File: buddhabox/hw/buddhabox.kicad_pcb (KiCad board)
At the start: 2 copper layers, 48.3 x 22.9 mm, 53 parts, among them J1 Serial, J2 SWD, J3 USB_B_Micro, J4 Speaker, J5 Battery, SW1 SW_Push, SW3 SW_Push, SW4 SW_Push, U1 TPS61291DRVR, U3 RP2040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

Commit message: Updated with working board design and pictures.
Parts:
- removed D2: LED Red, LED_SMD:LED_0603_1608Metric
- removed R5: 1k, Resistor_SMD:R_0402_1005Metric
- moved D3 16.8 mm to (129.1, 103.5), turned to -90 degrees
- moved C20 1.40 mm to (126.6, 118.0)
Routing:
- net Net-(D3-Pad2): track 1.51 -> 20.9 mm, vias 0 -> 2
- net +3.3V: track 107.9 -> 103.9 mm
- net GND: track 36.9 -> 35.5 mm
- net Net-(D2-Pad2): track 1.24 -> 0.00 mm
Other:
- board text removed: "PWR"

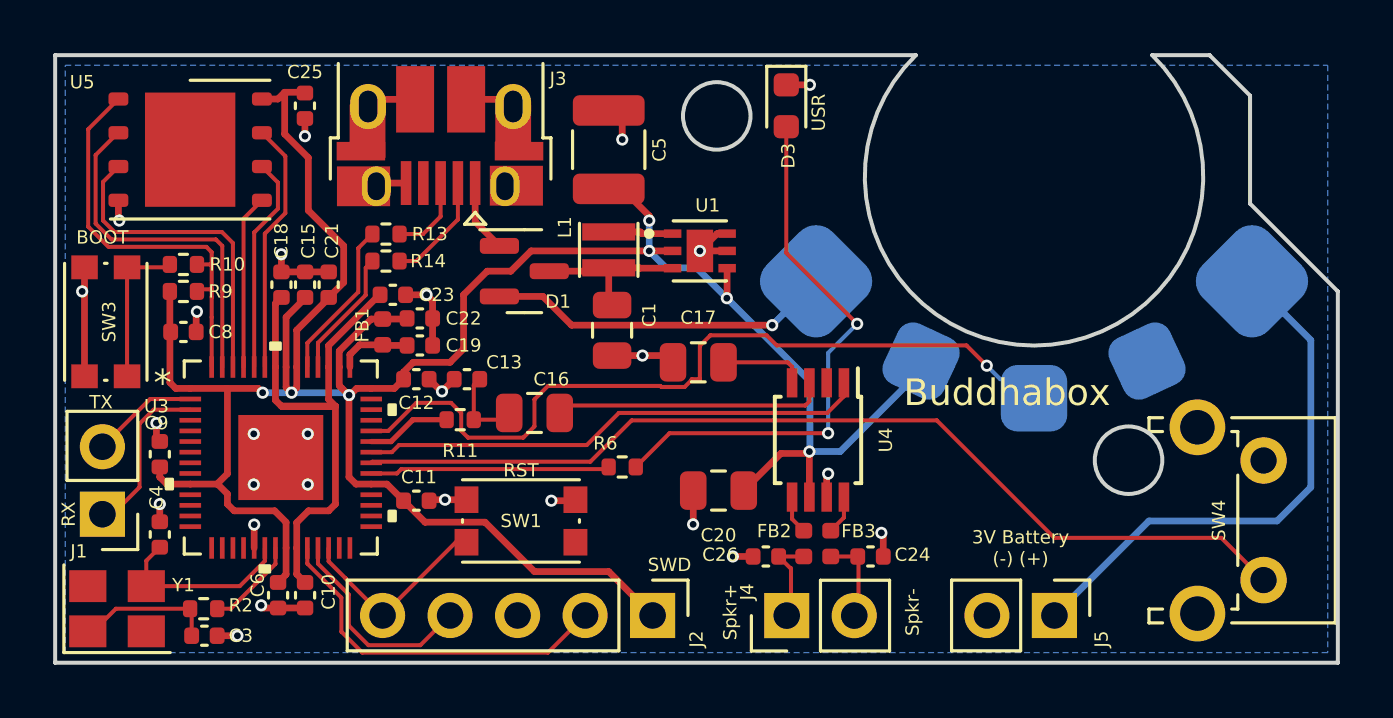
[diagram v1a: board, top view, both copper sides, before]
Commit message: switch to i2s amp & added LDO to vbus
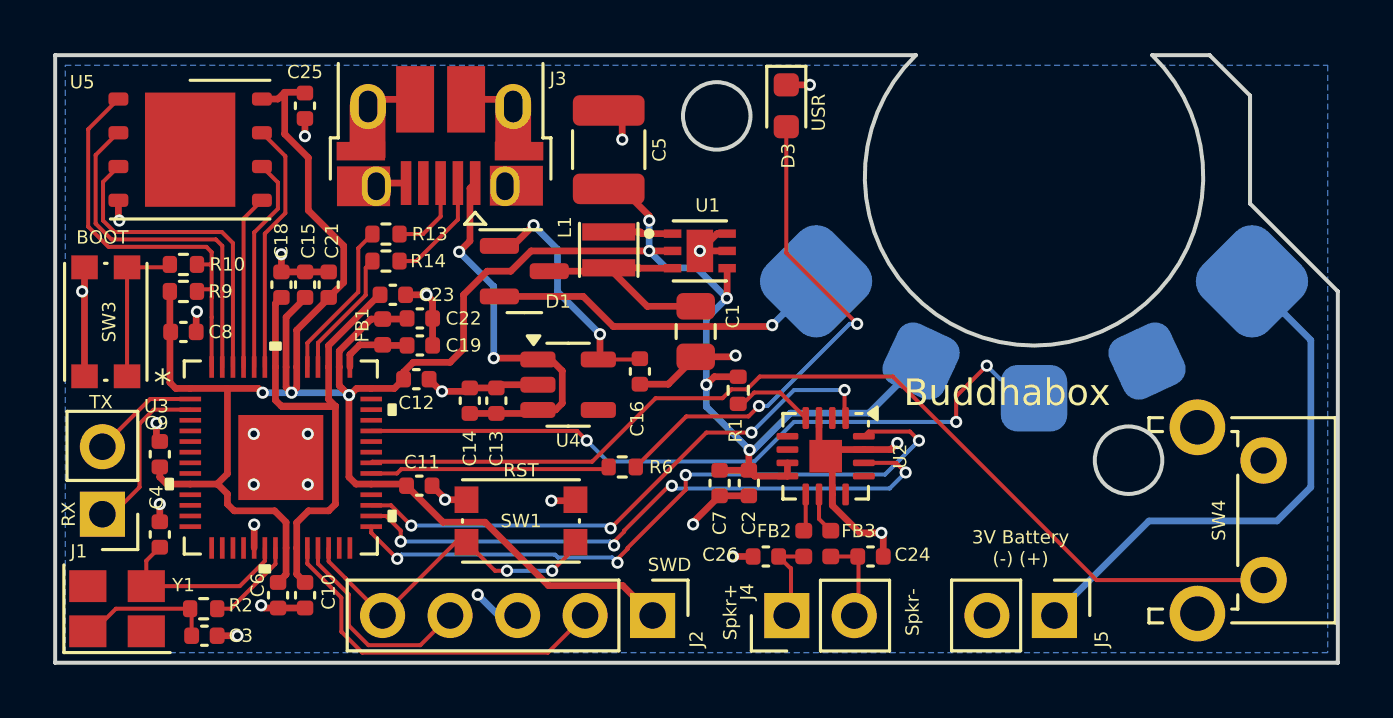
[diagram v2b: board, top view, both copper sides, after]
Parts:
- removed C17, C20: 10uf, Capacitor_SMD:C_0805_2012Metric
- removed R11: 100, Resistor_SMD:R_0402_1005Metric
- removed Ref**: Val**, emeb_library:avatar
- added C14: 1u, Capacitor_SMD:C_0402_1005Metric, F.Cu at (117.2, 114.6)
- added C2: 10uf, Capacitor_SMD:C_0402_1005Metric, F.Cu at (127.7, 117.7)
- added C7: 0.1uf, Capacitor_SMD:C_0402_1005Metric, F.Cu at (126.6, 117.7)
- added R1: 10k, Resistor_SMD:R_0402_1005Metric, F.Cu at (127.3, 114.2)
- added U2: MAX98357A, Package_DFN_QFN:TQFN-16-1EP_3x3mm_P0.5mm_EP1.23x1.23mm, F.Cu at (130.6, 116.7)
- C13: value 0.1uf -> 100nf
- C16: footprint Capacitor_SMD:C_0805_2012Metric -> Capacitor_SMD:C_0402_1005Metric
- U4: value PAM8302AAD -> ME6211C; footprint Package_SO:TSSOP-8_3x3mm_P0.65mm -> Package_TO_SOT_SMD:SOT-23-5
- moved U4 9.63 mm to (120.9, 114.0), turned to 0 degrees
- moved C16 4.26 mm to (123.6, 113.5), turned to -90 degrees
- moved C1 3.15 mm to (125.7, 112.0)
- moved C13 1.37 mm to (118.2, 114.6), turned to 90 degrees
- moved C11 0.57 mm to (115.3, 117.8)
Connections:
- C13 pad 1: Net-(C13-Pad1) -> Vbus
- C16 pad 1: Net-(C13-Pad1) -> /VBus3v3
- C16 pad 2: Net-(C16-Pad2) -> GND
- D1 pad 1: Vbus -> /VBus3v3
- FB2 pad 1: Net-(FB2-Pad1) -> Net-(U2-OUTP)
- FB3 pad 1: Net-(FB3-Pad1) -> Net-(U2-OUTN)
- U3 pad 29: unconnected-(U3-Pad29) -> BCLK
- U3 pad 30: unconnected-(U3-Pad30) -> LRCLK
- U3 pad 31: unconnected-(U3-Pad31) -> DIN
- U3 pad 37: /PDM+ -> unconnected-(U3-GPIO25-Pad37)
- U4 pad 1: /SD -> Vbus
- U4 pad 2: unconnected-(U4-Pad2) -> GND
- U4 pad 3: Net-(C16-Pad2) -> Vbus
- U4 pad 4: Net-(C17-Pad2) -> (no net)
- U4 pad 5: Net-(FB2-Pad1) -> /VBus3v3
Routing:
- net BCLK: track 0.00 -> 26.1 mm, vias 0 -> 4
- net LRCLK: track 0.00 -> 23.9 mm, vias 0 -> 4
- net DIN: track 0.00 -> 21.4 mm, vias 0 -> 4
- net /SD: track 19.2 -> 0.00 mm
- net GND: track 35.5 -> 51.2 mm, vias 26 -> 27
- net Vbus: track 2.74 -> 15.0 mm, vias 0 -> 2
- net Net-(C16-Pad2): track 10.3 -> 0.00 mm
- net /VBus3v3: track 0.00 -> 9.29 mm, vias 0 -> 2
- net /NRST: track 7.68 -> 12.8 mm, vias 0 -> 2
- net Net-(C17-Pad2): track 3.25 -> 0.00 mm
- net /PDM+: track 3.18 -> 0.00 mm
- net Net-(U2-~{SD_MODE}): track 0.00 -> 3.11 mm
- net Net-(C13-Pad1): track 3.06 -> 0.00 mm
- net /Vraw: track 6.15 -> 8.57 mm
- net /POT: track 29.2 -> 27.0 mm, vias 1 -> 3
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
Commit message: updated schematic with lcsc part numbers
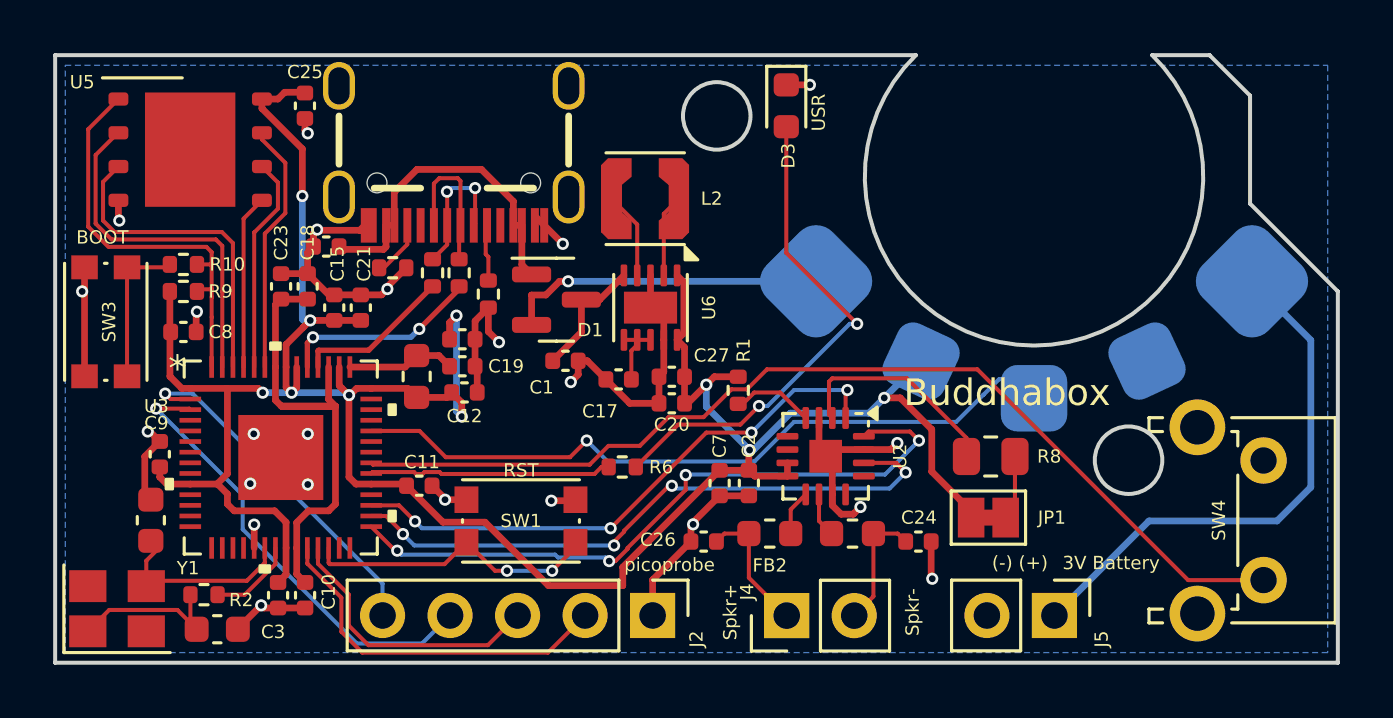
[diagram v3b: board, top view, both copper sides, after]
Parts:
- removed C13: 100nf, Capacitor_SMD:C_0402_1005Metric
- removed C14: 1u, Capacitor_SMD:C_0402_1005Metric
- removed C16: 10uf, Capacitor_SMD:C_0402_1005Metric
- removed J1: Serial, Connector_PinHeader_2.54mm:PinHeader_1x02_P2.54mm_Vertical
- removed J3: USB_B_Micro, Connector_USB:USB_Micro-B_Amphenol_10103594-0001LF_Horizontal
- removed L1: 3.3uH, Inductor_SMD:L_Taiyo-Yuden_MD-2020
- removed R13, R14: 27.5, Resistor_SMD:R_0402_1005Metric
- removed U1: TPS61291DRVR, emeb_library:SON65P200X200X80-7N
- removed U4: ME6211C, Package_TO_SOT_SMD:SOT-23-5
- added C17: 0.1uf, Capacitor_SMD:C_0402_1005Metric, F.Cu at (122.8, 113.8)
- added C20: 10uf, Capacitor_SMD:C_0402_1005Metric, F.Cu at (124.8, 114.7)
- added C27: 10uf, Capacitor_SMD:C_0402_1005Metric, F.Cu at (124.8, 113.7)
- added J7: USB_C_Receptacle_USB2.0, MyLibrary:USB-C_SMD-TYPE-C-31-M-12, F.Cu at (116.6, 103.5)
- added JP1: Jumper_2_Bridged, Jumper:SolderJumper-2_P1.3mm_Bridged_Pad1.0x1.5mm, F.Cu at (136.7, 119.0)
- added L2: 1.5uH, Inductor_SMD:L_Coilcraft_LPS3010, F.Cu at (123.8, 107.0)
- added R3: 5.1k, Resistor_SMD:R_0402_1005Metric, F.Cu at (114.3, 109.6)
- added R4: 5.1k, Resistor_SMD:R_0402_1005Metric, F.Cu at (117.9, 110.6)
- added R5: 27.4, Resistor_SMD:R_0402_1005Metric, F.Cu at (115.8, 109.8)
- added R7: 27.4, Resistor_SMD:R_0402_1005Metric, F.Cu at (116.8, 109.8)
- added R8: 100k, Resistor_SMD:R_0805_2012Metric, F.Cu at (136.8, 116.7)
- added U6: TPS63031DSK, Package_SON:WSON-10-1EP_2.5x2.5mm_P0.5mm_EP1.2x2mm, F.Cu at (124.0, 111.1)
- C1: footprint Capacitor_SMD:C_0805_2012Metric -> Capacitor_SMD:C_0402_1005Metric
- C3, C4: value 27pf -> 30pf; footprint Capacitor_SMD:C_0402_1005Metric -> Capacitor_SMD:C_0603_1608Metric
- C5: value 22uf -> 10uf; footprint Capacitor_SMD:C_1210_3225Metric -> Capacitor_SMD:C_0402_1005Metric
- FB1, FB2, FB3: value 1k -> 600@100mhz; footprint Inductor_SMD:L_0402_1005Metric -> Inductor_SMD:L_0603_1608Metric
- J2: value SWD -> PICOPROBE
- SW4: value SW_Push -> SW_PushSide
- U5: value W25Q32JVZPIQ -> W25Q64JVZPIQ
- moved C5 11.2 mm to (111.8, 108.8), turned to 180 degrees
- moved C1 5.02 mm to (120.8, 113.1), turned to 0 degrees
- moved C23 4.22 mm to (110.1, 110.3), turned to 90 degrees
- moved C26 2.41 mm to (126.0, 119.9)
- moved FB1 2.11 mm to (115.2, 113.7), turned to -90 degrees
- moved C24 1.89 mm to (134.1, 119.9)
- moved C12 1.88 mm to (117.0, 114.3)
- moved C22 1.78 mm to (116.9, 112.3)
- moved C19 1.78 mm to (116.9, 113.3)
- moved D1 1.62 mm to (120.5, 110.8)
- moved C21 1.49 mm to (113.1, 111.1)
- moved C15 1.40 mm to (112.1, 111.1)
- moved FB2 1.33 mm to (128.5, 119.6), turned to 180 degrees
- moved C18 0.99 mm to (111.1, 110.3)
- moved FB3 0.90 mm to (131.6, 119.6), turned to 0 degrees
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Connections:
- C5 pad 1: +3.3V -> Vbus
- D1 pad 1: /VBus3v3 -> Vbus
- J2 pad 1: +3.3V -> GND
- J2 pad 3: GND -> /SWDIO
- J2 pad 4: /SWDIO -> /UART0_RX
- J2 pad 5: /NRST -> /UART0_TX
- U3 pad 46: Net-(U3-USB_DM) -> usb_D-
- U3 pad 47: Net-(U3-USB_DP) -> usb_D+
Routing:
- net /UART0_RX: track 6.34 -> 17.2 mm, vias 0 -> 1
- net /UART0_TX: track 4.05 -> 13.4 mm, vias 0 -> 1
- net /VBus3v3: track 9.29 -> 0.00 mm, vias 2 -> 0
- net Net-(U2-GAIN_SLOT): track 0.00 -> 8.27 mm
- net usb_D+: track 0.00 -> 7.56 mm, vias 0 -> 2
- net GND: track 51.2 -> 57.7 mm, vias 27 -> 23
- net Net-(U3-USB_DP): track 6.02 -> 0.00 mm
- net usb_D-: track 0.00 -> 5.92 mm
- net +3.3V: track 106.0 -> 100.5 mm, vias 8 -> 10
- net Net-(J7-D--PadA7): track 0.00 -> 5.30 mm, vias 0 -> 2
- net Net-(J7-D+-PadA6): track 0.00 -> 5.00 mm
- net Net-(U3-USB_DM): track 4.84 -> 0.00 mm
- net Net-(J3-D-): track 4.21 -> 0.00 mm
- net /Vraw: track 8.57 -> 4.73 mm
- net Net-(U6-L1): track 0.00 -> 3.29 mm
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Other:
- board text added: "(-) (+)"
- board text added: "3V Battery"
- board text added: "Buddhabox V0.2 (c) 2022 E. Brombaugh (c) 2024 J. Brodsky"
- board text added: "picoprobe"
- board text removed: "3V Battery (-) (+)"
- board text removed: "Buddhabox V0.1 (c) 2022 E. Brombaugh"
- board text removed: "RX"
- board text removed: "SWD"
- board text removed: "TX"
